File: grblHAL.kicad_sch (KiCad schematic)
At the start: 22 parts, among them J1 Screw_Terminal_01x08, J10 Screw_Terminal_01x08, J11 Screw_Terminal_01x04x3, J12 Screw_Terminal_01x02, J2 Screw_Terminal_01x08, J3 Screw_Terminal_01x08, J4 Screw_Terminal_01x06, J5 Screw_Terminal_01x06, J6 Screw_Terminal_01x02, J7 Screw_Terminal_01x08, J8 Screw_Terminal_01x02, J9 Screw_Terminal_01x08

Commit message: added lcsc field so that bom can match during jlcpcb fab
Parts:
- J1, J10, J2, J3, J7, J9: LCSC (none) -> C14235
- J11: LCSC (none) -> C7245
- J12, J6, J8: LCSC (none) -> C8387
- J4, J5: LCSC (none) -> C7246
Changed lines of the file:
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@@
 			)
 		)
+		(property "LCSC" "C14235"
+			(at 351.79 92.71 0)
+			(effects
+				(font
+					(size 1.27 1.27)
+				)
+				(hide yes)
+			)
+		)
 		(pin "5"
 		)
@@
 			)
 		)
+		(property "LCSC" "C7246"
+			(at 57.15 156.21 0)
+			(effects
+				(font
+					(size 1.27 1.27)
+				)
+				(hide yes)
+			)
+		)
 		(pin "5"
 		)
@@
 			)
 		)
+		(property "LCSC" "C8387"
+			(at 100.33 133.35 0)
+			(effects
+				(font
+					(size 1.27 1.27)
+				)
+				(hide yes)
+			)
+		)
 		(pin "1"
 		)
@@
 			)
 		)
+		(property "LCSC" "C14235"
+			(at 27.94 97.79 0)
+			(effects
+				(font
+					(size 1.27 1.27)
+				)
+				(hide yes)
+			)
+		)
 		(pin "5"
 		)
@@
 			)
 		)
+		(property "LCSC" "C8387"
+			(at 327.66 105.41 0)
+			(effects
+				(font
+					(size 1.27 1.27)
+				)
+				(hide yes)
+			)
+		)
 		(pin "2"
 		)
@@
 			)
 		)
+		(property "LCSC" "C14235"
+			(at 27.94 66.04 0)
+			(effects
+				(font
+					(size 1.27 1.27)
+				)
+				(hide yes)
+			)
+		)
 		(pin "5"
 		)
@@
 			)
 		)
+		(property "LCSC" "C14235"
+			(at 309.88 149.86 0)
+			(effects
+				(font
+					(size 1.27 1.27)
+				)
+				(hide yes)
+			)
+		)
 		(pin "5"
 		)
@@
 			)
 		)
+		(property "LCSC" "C7246"
+			(at 72.39 146.05 0)
+			(effects
+				(font
+					(size 1.27 1.27)
+				)
+				(hide yes)
+			)
+		)
 		(pin "5"
 		)
@@
 			)
 		)
+		(property "LCSC" "C8387"
+			(at 355.6 125.73 0)
+			(effects
+				(font
+					(size 1.27 1.27)
+				)
+				(hide yes)
+			)
+		)
 		(pin "2"
 		)
@@
 			)
 		)
+		(property "LCSC" "C7245"
+			(at 355.6 118.11 0)
+			(effects
+				(font
+					(size 1.27 1.27)
+				)
+				(hide yes)
+			)
+		)
 		(pin "3"
 		)
@@
 			)
 		)
+		(property "LCSC" "C14235"
+			(at 336.55 74.93 0)
+			(effects
+				(font
+					(size 1.27 1.27)
+				)
+				(hide yes)
+			)
+		)
 		(pin "5"
 		)
@@
 			(at 27.94 36.83 0)
 			(effects
+				(font
+					(size 1.27 1.27)
+				)
+				(hide yes)
+			)
+		)
+		(property "LCSC" "C14235"
+			(at 27.94 36.83 0)
+			(effects

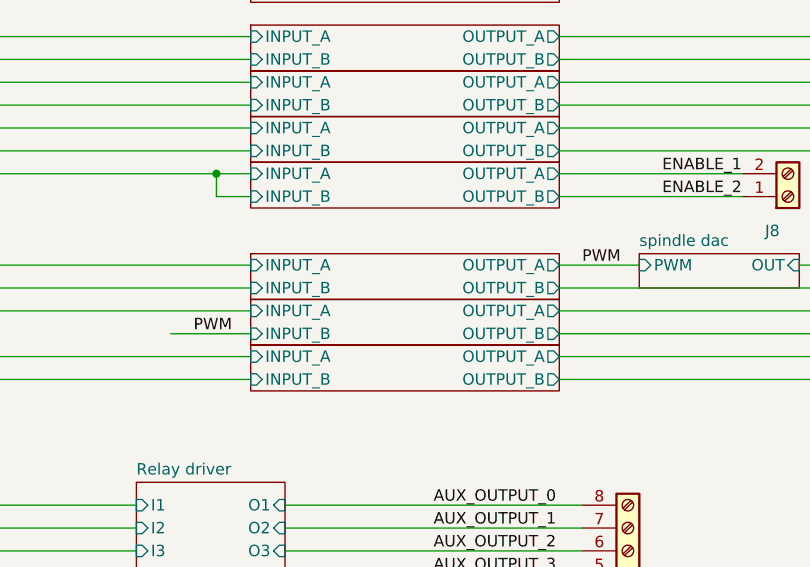
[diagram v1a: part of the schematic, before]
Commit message: moved rs485 re/de lines, start of manual
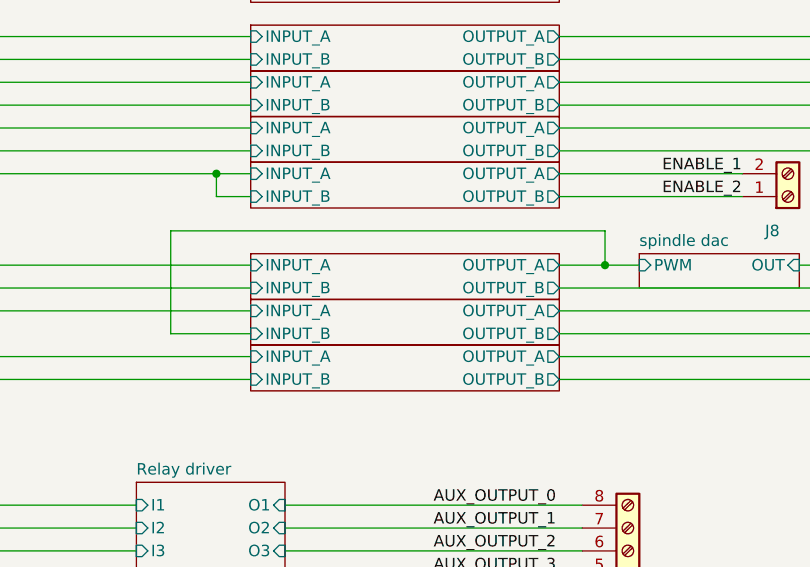
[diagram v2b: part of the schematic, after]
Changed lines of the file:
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@@
+	)
+	(junction
+		(at 307.34 113.03)
+		(diameter 0)
+		(color 0 0 0 0)
 	)
 	(junction
@@
 	(wire
 		(pts
+			(xy 307.34 113.03) (xy 311.15 113.03)
+		)
+		(stroke
+			(width 0)
+			(type default)
+		)
+	)
+	(wire
+		(pts
 			(xy 146.05 120.65) (xy 146.05 118.11)
 		)
@@
 	(wire
 		(pts
-			(xy 302.26 113.03) (xy 311.15 113.03)
+			(xy 302.26 113.03) (xy 307.34 113.03)
 		)
 		(stroke
@@
 	(wire
 		(pts
+			(xy 259.08 109.22) (xy 307.34 109.22)
+		)
+		(stroke
+			(width 0)
+			(type default)
+		)
+	)
+	(wire
+		(pts
 			(xy 118.11 74.93) (xy 118.11 76.2)
 		)
@@
 	(wire
 		(pts
+			(xy 307.34 109.22) (xy 307.34 113.03)
+		)
+		(stroke
+			(width 0)
+			(type default)
+		)
+	)
+	(wire
+		(pts
 			(xy 146.05 74.93) (xy 147.32 74.93)
 		)
@@
 		(pts
 			(xy 172.72 71.12) (xy 171.45 71.12)
+		)
+		(stroke
+			(width 0)
+			(type default)
+		)
+	)
+	(wire
+		(pts
+			(xy 259.08 120.65) (xy 259.08 109.22)
 		)
 		(stroke
@@
 		)
 	)
-	(label "PWM"
-		(at 261.62 120.65 0)
-		(effects
-			(font
-				(size 1.27 1.27)
-			)
-			(justify left bottom)
-		)
-	)
 	(label "STP_Y"
 		(at 322.58 77.47 0)
@@
 		(effects
 			(font
-				(size 1.27 1.27)
-			)
-			(justify left bottom)
-		)
-	)
-	(label "PWM"
-		(at 304.8 113.03 0)
-		(effects
-			(font

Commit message: added mating push in connectors to BOM
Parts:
- added J45, J46, J47, J48, J49, J50: Screw_Terminal_01x08, symbol Connector:Screw_Terminal_01x08
- added J51, J52: ~, symbol Connector:Screw_Terminal_01x06
- added J53, J54: ~, symbol Connector:Screw_Terminal_01x02
- added J55: ~, symbol Connector:Screw_Terminal_01x04
- J1: Notes matching push in block is WJ15EDGK-3.81-8P -> matching push in block is #C14234 WJ15EDGK-3.81-8P
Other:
- moved on the sheet: J5, J9
